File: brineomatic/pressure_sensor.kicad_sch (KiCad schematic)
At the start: 8 parts, among them J5 Conn_01x02

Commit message: getting closer.  added tds
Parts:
- renumbered C1 to C17, D1 to D18, J5 to J12, JP1 to JP2, R1 to R31, R9 to R32, R10 to R33, R2 to R34
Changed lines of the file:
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@@
 		(dnp no)
 		(fields_autoplaced yes)
-		(property "Reference" "#PWR01"
+		(property "Reference" "#PWR036"
 			(at 96.52 77.47 0)
 			(effects
@@
 		)
 		(instances
-			(project ""
-				(path "/96477ae2-ef08-48f3-8dd4-fe4478541f68/e7fd98b0-0753-4e9e-b57d-135c0c1a0b39"
-					(reference "#PWR01")
+			(project "brineomatic"
+				(path "/96477ae2-ef08-48f3-8dd4-fe4478541f68/c8ab4709-9ad5-4833-bb93-07e00d6a0170"
+					(reference "#PWR036")
+					(unit 1)
+				)
+				(path "/96477ae2-ef08-48f3-8dd4-fe4478541f68/e7fd98b0-0753-4e9e-b57d-135c0c1a0b39"
+					(reference "#PWR?")
 					(unit 1)
 				)
@@
 		(dnp no)
 		(fields_autoplaced yes)
-		(property "Reference" "JP1"
+		(property "Reference" "JP2"
 			(at 129.54 81.28 0)
 			(effects
@@
 		)
 		(instances
-			(project ""
-				(path "/96477ae2-ef08-48f3-8dd4-fe4478541f68/e7fd98b0-0753-4e9e-b57d-135c0c1a0b39"
-					(reference "JP1")
+			(project "brineomatic"
+				(path "/96477ae2-ef08-48f3-8dd4-fe4478541f68/c8ab4709-9ad5-4833-bb93-07e00d6a0170"
+					(reference "JP2")
+					(unit 1)
+				)
+				(path "/96477ae2-ef08-48f3-8dd4-fe4478541f68/e7fd98b0-0753-4e9e-b57d-135c0c1a0b39"
+					(reference "JP?")
 					(unit 1)
 				)
@@
 		(dnp no)
 		(fields_autoplaced yes)
-		(property "Reference" "#PWR05"
+		(property "Reference" "#PWR038"
 			(at 144.78 77.47 0)
 			(effects
@@
 		)
 		(instances
-			(project ""
-				(path "/96477ae2-ef08-48f3-8dd4-fe4478541f68/e7fd98b0-0753-4e9e-b57d-135c0c1a0b39"
-					(reference "#PWR05")
+			(project "brineomatic"
+				(path "/96477ae2-ef08-48f3-8dd4-fe4478541f68/c8ab4709-9ad5-4833-bb93-07e00d6a0170"
+					(reference "#PWR038")
+					(unit 1)
+				)
+				(path "/96477ae2-ef08-48f3-8dd4-fe4478541f68/e7fd98b0-0753-4e9e-b57d-135c0c1a0b39"
+					(reference "#PWR?")
 					(unit 1)
 				)
@@
 		(dnp no)
 		(fields_autoplaced yes)
-		(property "Reference" "#PWR02"
+		(property "Reference" "#PWR037"
 			(at 96.52 114.3 0)
 			(effects
@@
 		(instances
 			(project "brineomatic"
+				(path "/96477ae2-ef08-48f3-8dd4-fe4478541f68/c8ab4709-9ad5-4833-bb93-07e00d6a0170"
+					(reference "#PWR037")
+					(unit 1)
+				)
 				(path "/96477ae2-ef08-48f3-8dd4-fe4478541f68/e7fd98b0-0753-4e9e-b57d-135c0c1a0b39"
 					(reference "#PWR02")
@@
 		(dnp no)
 		(fields_autoplaced yes)
-		(property "Reference" "D1"
+		(property "Reference" "D18"
 			(at 147.32 86.36 90)
 			(effects
@@
 		(instances
 			(project "brineomatic"
+				(path "/96477ae2-ef08-48f3-8dd4-fe4478541f68/c8ab4709-9ad5-4833-bb93-07e00d6a0170"
+					(reference "D18")
+					(unit 1)
+				)
 				(path "/96477ae2-ef08-48f3-8dd4-fe4478541f68/e7fd98b0-0753-4e9e-b57d-135c0c1a0b39"
 					(reference "D1")
@@
 		(dnp no)
 		(fields_autoplaced yes)
-		(property "Reference" "R9"
+		(property "Reference" "R32"
 			(at 124.46 90.17 0)
 			(effects
@@
 		(instances
 			(project "brineomatic"
+				(path "/96477ae2-ef08-48f3-8dd4-fe4478541f68/c8ab4709-9ad5-4833-bb93-07e00d6a0170"
+					(reference "R32")
+					(unit 1)
+				)
 				(path "/96477ae2-ef08-48f3-8dd4-fe4478541f68/e7fd98b0-0753-4e9e-b57d-135c0c1a0b39"
 					(reference "R9")
@@
 		(dnp no)
 		(fields_autoplaced yes)
-		(property "Reference" "J5"
+		(property "Reference" "J12"
 			(at 87.63 78.74 0)
 			(effects
@@
 		)
 		(instances
-			(project ""
-				(path "/96477ae2-ef08-48f3-8dd4-fe4478541f68/e7fd98b0-0753-4e9e-b57d-135c0c1a0b39"
-					(reference "J5")
+			(project "brineomatic"
+				(path "/96477ae2-ef08-48f3-8dd4-fe4478541f68/c8ab4709-9ad5-4833-bb93-07e00d6a0170"
+					(reference "J12")
+					(unit 1)
+				)
+				(path "/96477ae2-ef08-48f3-8dd4-fe4478541f68/e7fd98b0-0753-4e9e-b57d-135c0c1a0b39"
+					(reference "J?")
 					(unit 1)
 				)
@@
 		(dnp no)
 		(fields_autoplaced yes)
-		(property "Reference" "R2"
+		(property "Reference" "R34"
 			(at 158.75 81.28 90)
 			(effects
@@
 		(instances
 			(project "brineomatic"
+				(path "/96477ae2-ef08-48f3-8dd4-fe4478541f68/c8ab4709-9ad5-4833-bb93-07e00d6a0170"
+					(reference "R34")
+					(unit 1)
+				)
 				(path "/96477ae2-ef08-48f3-8dd4-fe4478541f68/e7fd98b0-0753-4e9e-b57d-135c0c1a0b39"
 					(reference "R2")
@@
 		(dnp no)
 		(fields_autoplaced yes)
-		(property "Reference" "R10"
+		(property "Reference" "R33"
 			(at 124.46 97.79 0)
 			(effects
@@
 		(instances
 			(project "brineomatic"
+				(path "/96477ae2-ef08-48f3-8dd4-fe4478541f68/c8ab4709-9ad5-4833-bb93-07e00d6a0170"
+					(reference "R33")
+					(unit 1)
+				)
 				(path "/96477ae2-ef08-48f3-8dd4-fe4478541f68/e7fd98b0-0753-4e9e-b57d-135c0c1a0b39"
 					(reference "R10")
@@
 		(dnp no)
 		(fields_autoplaced yes)
-		(property "Reference" "R1"
+		(property "Reference" "R31"
 			(at 99.06 91.44 0)
 			(effects
@@
 		(instances
 			(project "brineomatic"
+				(path "/96477ae2-ef08-48f3-8dd4-fe4478541f68/c8ab4709-9ad5-4833-bb93-07e00d6a0170"
+					(reference "R31")
+					(unit 1)
+				)
 				(path "/96477ae2-ef08-48f3-8dd4-fe4478541f68/e7fd98b0-0753-4e9e-b57d-135c0c1a0b39"
 					(reference "R1")
@@
 		(on_board yes)
 		(dnp no)
-		(property "Reference" "C1"
+		(property "Reference" "C17"
 			(at 166.37 96.5263 0)
 			(effects
@@
 		(instances
 			(project "brineomatic"
+				(path "/96477ae2-ef08-48f3-8dd4-fe4478541f68/c8ab4709-9ad5-4833-bb93-07e00d6a0170"
+					(reference "C17")
+					(unit 1)
+				)
 				(path "/96477ae2-ef08-48f3-8dd4-fe4478541f68/e7fd98b0-0753-4e9e-b57d-135c0c1a0b39"
 					(reference "C1")

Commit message: starting to shape up, footprints etc
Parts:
- J12: value Conn_01x02 -> SENSOR; footprint (none) -> TerminalBlock_Phoenix:TerminalBlock_Phoenix_PT-1,5-2-3.5-H_1x02_P3.50mm_Horizontal
- JP2: footprint (none) -> Jumper:SolderJumper-2_P1.3mm_Open_RoundedPad1.0x1.5mm
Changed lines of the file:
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@@
 		(dnp no)
 		(fields_autoplaced yes)
-		(property "Reference" "#PWR036"
+		(property "Reference" "#PWR035"
 			(at 96.52 77.47 0)
 			(effects
@@
 			(project "brineomatic"
 				(path "/96477ae2-ef08-48f3-8dd4-fe4478541f68/c8ab4709-9ad5-4833-bb93-07e00d6a0170"
-					(reference "#PWR036")
-					(unit 1)
-				)
-				(path "/96477ae2-ef08-48f3-8dd4-fe4478541f68/e7fd98b0-0753-4e9e-b57d-135c0c1a0b39"
-					(reference "#PWR?")
+					(reference "#PWR035")
+					(unit 1)
+				)
+				(path "/96477ae2-ef08-48f3-8dd4-fe4478541f68/e7fd98b0-0753-4e9e-b57d-135c0c1a0b39"
+					(reference "#PWR06")
 					(unit 1)
 				)
@@
 			)
 		)
-		(property "Footprint" ""
+		(property "Footprint" "Jumper:SolderJumper-2_P1.3mm_Open_RoundedPad1.0x1.5mm"
 			(at 129.54 87.63 0)
 			(effects
@@
 				)
 				(path "/96477ae2-ef08-48f3-8dd4-fe4478541f68/e7fd98b0-0753-4e9e-b57d-135c0c1a0b39"
-					(reference "JP?")
+					(reference "JP1")
 					(unit 1)
 				)
@@
 		(dnp no)
 		(fields_autoplaced yes)
-		(property "Reference" "#PWR038"
+		(property "Reference" "#PWR037"
 			(at 144.78 77.47 0)
 			(effects
@@
 			(project "brineomatic"
 				(path "/96477ae2-ef08-48f3-8dd4-fe4478541f68/c8ab4709-9ad5-4833-bb93-07e00d6a0170"
-					(reference "#PWR038")
-					(unit 1)
-				)
-				(path "/96477ae2-ef08-48f3-8dd4-fe4478541f68/e7fd98b0-0753-4e9e-b57d-135c0c1a0b39"
-					(reference "#PWR?")
+					(reference "#PWR037")
+					(unit 1)
+				)
+				(path "/96477ae2-ef08-48f3-8dd4-fe4478541f68/e7fd98b0-0753-4e9e-b57d-135c0c1a0b39"
+					(reference "#PWR08")
 					(unit 1)
 				)
@@
 		(dnp no)
 		(fields_autoplaced yes)
-		(property "Reference" "#PWR037"
+		(property "Reference" "#PWR036"
 			(at 96.52 114.3 0)
 			(effects
@@
 			(project "brineomatic"
 				(path "/96477ae2-ef08-48f3-8dd4-fe4478541f68/c8ab4709-9ad5-4833-bb93-07e00d6a0170"
-					(reference "#PWR037")
-					(unit 1)
-				)
-				(path "/96477ae2-ef08-48f3-8dd4-fe4478541f68/e7fd98b0-0753-4e9e-b57d-135c0c1a0b39"
-					(reference "#PWR02")
+					(reference "#PWR036")
+					(unit 1)
+				)
+				(path "/96477ae2-ef08-48f3-8dd4-fe4478541f68/e7fd98b0-0753-4e9e-b57d-135c0c1a0b39"
+					(reference "#PWR07")
 					(unit 1)
 				)
@@
 				)
 				(path "/96477ae2-ef08-48f3-8dd4-fe4478541f68/e7fd98b0-0753-4e9e-b57d-135c0c1a0b39"
-					(reference "R9")
+					(reference "R2")
 					(unit 1)
 				)
@@
 			)
 		)
-		(property "Value" "Conn_01x02"
+		(property "Value" "SENSOR"
 			(at 87.63 81.28 0)
 			(effects
@@
 			)
 		)
-		(property "Footprint" ""
+		(property "Footprint" "TerminalBlock_Phoenix:TerminalBlock_Phoenix_PT-1,5-2-3.5-H_1x02_P3.50mm_Horizontal"
 			(at 87.63 85.09 0)
 			(effects
@@
 				)
 				(path "/96477ae2-ef08-48f3-8dd4-fe4478541f68/e7fd98b0-0753-4e9e-b57d-135c0c1a0b39"
-					(reference "J?")
+					(reference "J1")
 					(unit 1)
 				)
@@
 				)
 				(path "/96477ae2-ef08-48f3-8dd4-fe4478541f68/e7fd98b0-0753-4e9e-b57d-135c0c1a0b39"
-					(reference "R2")
+					(reference "R4")
 					(unit 1)
 				)
@@
 				)
 				(path "/96477ae2-ef08-48f3-8dd4-fe4478541f68/e7fd98b0-0753-4e9e-b57d-135c0c1a0b39"
-					(reference "R10")
-					(unit 1)
-				)
+					(reference "R3")
+					(unit 1)
+				)

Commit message: starting to look good.
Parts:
- removed JP2: For Testing, Jumper:SolderJumper-2_P1.3mm_Open_RoundedPad1.0x1.5mm, symbol Jumper:SolderJumper_2_Open
- removed R32: 10.2K 0.1%, Resistor_SMD:R_1206_3216Metric_Pad1.30x1.75mm_HandSolder, symbol Device:R_Small_US
- removed R33: 19.8K 0.1%, Resistor_SMD:R_1206_3216Metric_Pad1.30x1.75mm_HandSolder, symbol Device:R_Small_US
- J12: value SENSOR -> PRESSURE; footprint TerminalBlock_Phoenix:TerminalBlock_Phoenix_PT-1,5-2-3.5-H_1x02_P3.50mm_Horizontal -> Connector_JST:JST_PH_S2B-PH-K_1x02_P2.00mm_Horizontal
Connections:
- net at J12.2 (Pin_2), R31.2: now also D18.3 (COM), R34.1
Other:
- moved on the sheet: C17, D18, R34

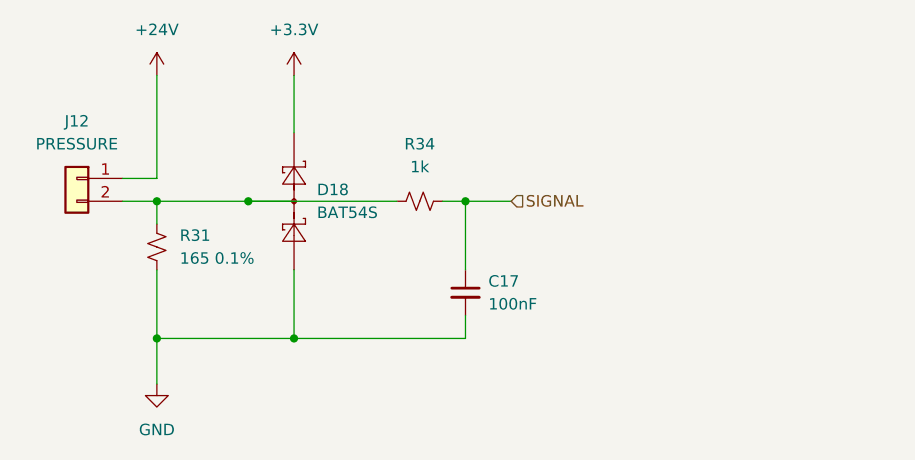
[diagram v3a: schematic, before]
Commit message: updated bom and prepping for Rev A
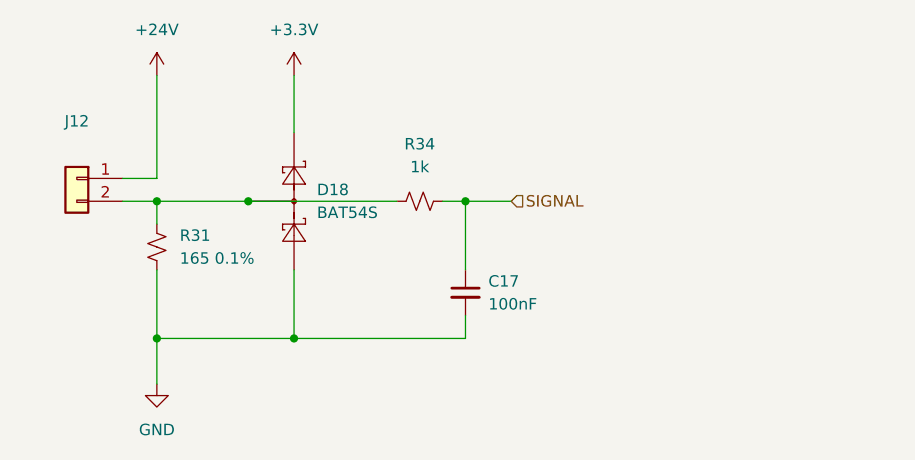
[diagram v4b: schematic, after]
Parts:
- J12: value PRESSURE -> ~; LCSC (none) -> C173752
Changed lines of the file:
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@@
 			)
 		)
-		(property "Value" "PRESSURE"
+		(property "Value" "~"
 			(at 87.63 81.28 0)
 			(effects
@@
 			(at 87.63 85.09 0)
 			(effects
+				(font
+					(size 1.27 1.27)
+				)
+				(hide yes)
+			)
+		)
+		(property "LCSC" "C173752"
+			(at 87.63 85.09 0)
+			(effects

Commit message: updates parts, footprints, etc.  ready for production.
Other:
- moved on the sheet: C17, R31
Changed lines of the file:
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@@
 	(wire
 		(pts
-			(xy 130.81 87.63) (xy 130.81 95.25)
+			(xy 130.81 87.63) (xy 130.81 92.71)
 		)
 		(stroke
@@
 	(wire
 		(pts
-			(xy 96.52 87.63) (xy 96.52 90.17)
+			(xy 96.52 87.63) (xy 96.52 92.71)
 		)
 		(stroke
@@
 	(wire
 		(pts
-			(xy 130.81 100.33) (xy 130.81 102.87)
+			(xy 130.81 97.79) (xy 130.81 102.87)
 		)
 		(stroke
@@
 	(wire
 		(pts
-			(xy 96.52 95.25) (xy 96.52 102.87)
+			(xy 96.52 97.79) (xy 96.52 102.87)
 		)
 		(stroke
@@
 	(symbol
 		(lib_id "Device:R_Small_US")
-		(at 96.52 92.71 180)
+		(at 96.52 95.25 180)
 		(unit 1)
 		(exclude_from_sim no)
@@
 		(fields_autoplaced yes)
 		(property "Reference" "R31"
-			(at 99.06 91.44 0)
+			(at 99.06 93.98 0)
 			(effects
 				(font
@@
 		)
 		(property "Value" "165 0.1%"
-			(at 99.06 93.98 0)
+			(at 99.06 96.52 0)
 			(effects
 				(font
@@
 		)
 		(property "Footprint" "Resistor_SMD:R_1206_3216Metric_Pad1.30x1.75mm_HandSolder"
-			(at 96.52 92.71 0)
+			(at 96.52 95.25 0)
 			(effects
 				(font
@@
 		)
 		(property "Datasheet" "~"
-			(at 96.52 92.71 0)
+			(at 96.52 95.25 0)
 			(effects
 				(font
@@
 		)
 		(property "Description" ""
-			(at 96.52 92.71 0)
+			(at 96.52 95.25 0)
 			(effects
 				(font
@@
 		)
 		(property "LCSC" "C870446"
-			(at 96.52 92.71 0)
+			(at 96.52 95.25 0)
 			(effects
 				(font
@@
 	(symbol
 		(lib_id "Device:C_Small")
-		(at 130.81 97.79 0)
+		(at 130.81 95.25 0)
 		(unit 1)
 		(exclude_from_sim no)
@@
 		(dnp no)
 		(property "Reference" "C17"
+			(at 133.35 93.9863 0)
+			(effects
+				(font
+					(size 1.27 1.27)
+				)
+				(justify left)
+			)
+		)
+		(property "Value" "100nF"
 			(at 133.35 96.5263 0)
 			(effects
@@
 			)
 		)
-		(property "Value" "100nF"
-			(at 133.35 99.0663 0)
-			(effects
-				(font
-					(size 1.27 1.27)
-				)
-				(justify left)
-			)
-		)
 		(property "Footprint" "Capacitor_SMD:C_0805_2012Metric_Pad1.18x1.45mm_HandSolder"
-			(at 130.81 97.79 0)
+			(at 130.81 95.25 0)
 			(effects
 				(font
@@
 		)
 		(property "Datasheet" "~"
-			(at 130.81 97.79 0)
+			(at 130.81 95.25 0)
 			(effects
 				(font
@@
 		)
 		(property "Description" ""
-			(at 130.81 97.79 0)
+			(at 130.81 95.25 0)
 			(effects
 				(font
@@
 		)
 		(property "Mouser" ""
-			(at 130.81 97.79 0)
+			(at 130.81 95.25 0)
 			(effects
 				(font
@@
 		)
 		(property "LCSC" "C49678"
-			(at 130.81 97.79 0)
-			(effects
-				(font
+			(at 130.81 95.25 0)
+			(effects
+				(font

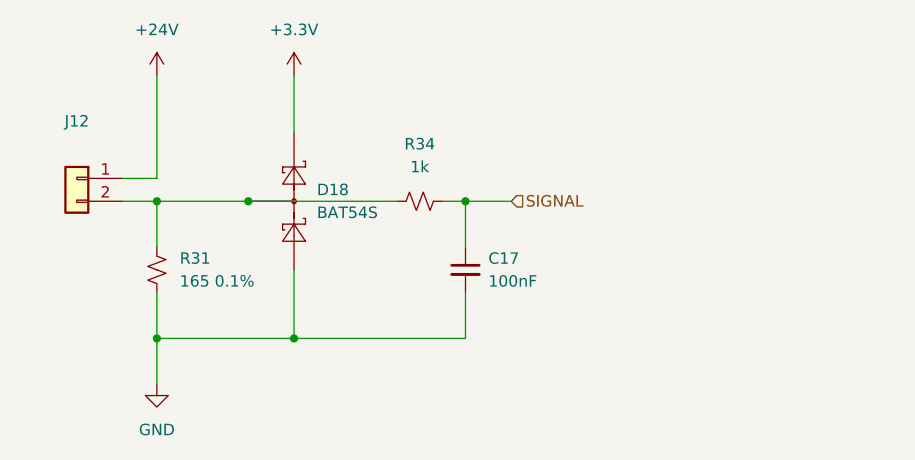
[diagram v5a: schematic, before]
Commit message: fixed bat54s placement.
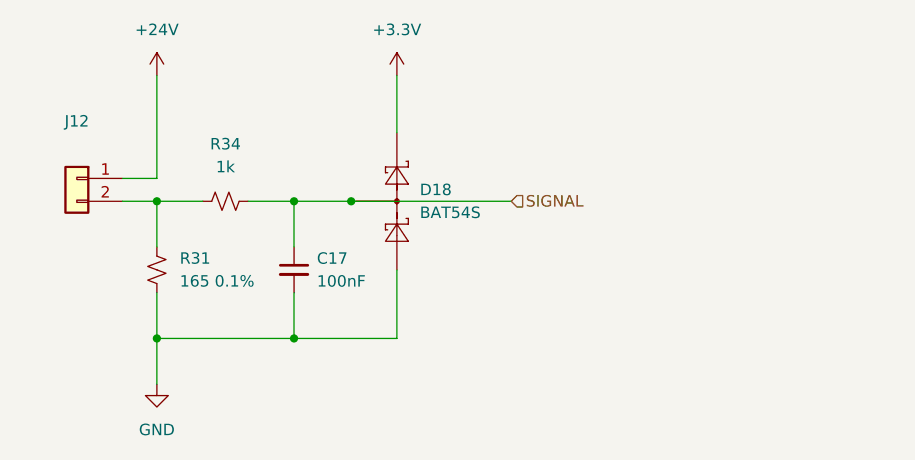
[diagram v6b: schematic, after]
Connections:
- net SIGNAL: now also D18.3 (COM)
- net at J12.2 (Pin_2), R31.2, R34.1: no longer D18.3 (COM)
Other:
- moved on the sheet: C17, D18, R34
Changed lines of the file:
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@@
 	(paper "A4")
+	(junction
+		(at 118.11 87.63)
+		(diameter 0)
+		(color 0 0 0 0)
+	)
+	(junction
+		(at 96.52 87.63)
+		(diameter 0)
+		(color 0 0 0 0)
+	)
 	(junction
 		(at 111.76 102.87)
@@
 	)
 	(junction
-		(at 130.81 87.63)
-		(diameter 0)
-		(color 0 0 0 0)
-	)
-	(junction
-		(at 96.52 87.63)
+		(at 111.76 87.63)
 		(diameter 0)
 		(color 0 0 0 0)
@@
 		(color 0 0 0 0)
 	)
-	(junction
-		(at 106.68 87.63)
-		(diameter 0)
-		(color 0 0 0 0)
-	)
-	(wire
-		(pts
-			(xy 130.81 87.63) (xy 135.89 87.63)
-		)
-		(stroke
-			(width 0)
-			(type default)
-		)
-	)
-	(wire
-		(pts
-			(xy 128.27 87.63) (xy 130.81 87.63)
-		)
-		(stroke
-			(width 0)
-			(type default)
-		)
-	)
-	(wire
-		(pts
-			(xy 111.76 73.66) (xy 111.76 80.01)
-		)
-		(stroke
-			(width 0)
-			(type default)
-		)
-	)
-	(wire
-		(pts
-			(xy 106.68 87.63) (xy 123.19 87.63)
-		)
-		(stroke
-			(width 0)
-			(type default)
-		)
-	)
-	(wire
-		(pts
-			(xy 111.76 102.87) (xy 111.76 95.25)
-		)
-		(stroke
-			(width 0)
-			(type default)
-		)
-	)
-	(wire
-		(pts
-			(xy 111.76 102.87) (xy 130.81 102.87)
+	(wire
+		(pts
+			(xy 111.76 87.63) (xy 118.11 87.63)
+		)
+		(stroke
+			(width 0)
+			(type default)
+		)
+	)
+	(wire
+		(pts
+			(xy 123.19 73.66) (xy 123.19 80.01)
+		)
+		(stroke
+			(width 0)
+			(type default)
+		)
+	)
+	(wire
+		(pts
+			(xy 123.19 102.87) (xy 123.19 95.25)
 		)
 		(stroke
@@
 	(wire
 		(pts
+			(xy 111.76 102.87) (xy 123.19 102.87)
+		)
+		(stroke
+			(width 0)
+			(type default)
+		)
+	)
+	(wire
+		(pts
 			(xy 92.71 87.63) (xy 96.52 87.63)
 		)
@@
 	(wire
 		(pts
-			(xy 130.81 87.63) (xy 130.81 92.71)
+			(xy 118.11 87.63) (xy 135.89 87.63)
+		)
+		(stroke
+			(width 0)
+			(type default)
+		)
+	)
+	(wire
+		(pts
+			(xy 111.76 87.63) (xy 111.76 92.71)
 		)
 		(stroke
@@
 	(wire
 		(pts
-			(xy 130.81 97.79) (xy 130.81 102.87)
+			(xy 111.76 97.79) (xy 111.76 102.87)
+		)
+		(stroke
+			(width 0)
+			(type default)
+		)
+	)
+	(wire
+		(pts
+			(xy 106.68 87.63) (xy 111.76 87.63)
 		)
 		(stroke
@@
 	(wire
 		(pts
-			(xy 96.52 87.63) (xy 106.68 87.63)
-		)
-		(stroke
-			(width 0)
-			(type default)
-		)
-	)
-	(wire
-		(pts
 			(xy 96.52 97.79) (xy 96.52 102.87)
+		)
+		(stroke
+			(width 0)
+			(type default)
+		)
+	)
+	(wire
+		(pts
+			(xy 96.52 87.63) (xy 101.6 87.63)
 		)
 		(stroke
@@
 	(symbol
 		(lib_id "power:+3.3V")
-		(at 111.76 73.66 0)
+		(at 123.19 73.66 0)
 		(unit 1)
 		(exclude_from_sim no)
@@
 		(fields_autoplaced yes)
 		(property "Reference" "#PWR037"
-			(at 111.76 77.47 0)
+			(at 123.19 77.47 0)
 			(effects
 				(font
@@
 		)
 		(property "Value" "+3.3V"
-			(at 111.76 68.58 0)
+			(at 123.19 68.58 0)
 			(effects
 				(font
@@
 		)
 		(property "Footprint" ""
-			(at 111.76 73.66 0)
+			(at 123.19 73.66 0)
 			(effects
 				(font
@@
 		)
 		(property "Datasheet" ""
-			(at 111.76 73.66 0)
+			(at 123.19 73.66 0)
 			(effects
 				(font
@@
 		)
 		(property "Description" "Power symbol creates a global label with name \"+3.3V\""
-			(at 111.76 73.66 0)
+			(at 123.19 73.66 0)
 			(effects
 				(font
@@
 	(symbol
 		(lib_id "Diode:BAT54S")
-		(at 111.76 87.63 270)
+		(at 123.19 87.63 270)
 		(mirror x)
 		(unit 1)
@@
 		(fields_autoplaced yes)
 		(property "Reference" "D18"
-			(at 114.3 86.36 90)
+			(at 125.73 86.36 90)
 			(effects
 				(font
@@
 		)
 		(property "Value" "BAT54S"
-			(at 114.3 88.9 90)
+			(at 125.73 88.9 90)
 			(effects
 				(font
@@
 		)
 		(property "Footprint" "Package_TO_SOT_SMD:SOT-23"
-			(at 114.935 85.725 0)
+			(at 126.365 85.725 0)
 			(effects
 				(font
@@
 		)
 		(property "Datasheet" "https://www.diodes.com/assets/Datasheets/ds11005.pdf"
-			(at 111.76 90.678 0)
+			(at 123.19 90.678 0)
 			(effects
 				(font
@@
 		)
 		(property "Description" ""
-			(at 111.76 87.63 0)
+			(at 123.19 87.63 0)
 			(effects
 				(font
@@
 		)
 		(property "LCSC" "C727126"
-			(at 111.76 87.63 90)
+			(at 123.19 87.63 90)
 			(effects
 				(font
@@
 	(symbol
 		(lib_id "Device:R_Small_US")
-		(at 125.73 87.63 90)
+		(at 104.14 87.63 90)
 		(unit 1)
 		(exclude_from_sim no)
@@
 		(fields_autoplaced yes)
 		(property "Reference" "R34"
-			(at 125.73 81.28 90)
+			(at 104.14 81.28 90)
 			(effects
 				(font
@@
 		)
 		(property "Value" "1k"
-			(at 125.73 83.82 90)
+			(at 104.14 83.82 90)
 			(effects
 				(font
@@
 		)
 		(property "Footprint" "Resistor_SMD:R_0805_2012Metric_Pad1.20x1.40mm_HandSolder"
-			(at 125.73 87.63 0)
+			(at 104.14 87.63 0)
 			(effects
 				(font
@@
 		)
 		(property "Datasheet" "~"
-			(at 125.73 87.63 0)
+			(at 104.14 87.63 0)
 			(effects
 				(font
@@
 		)
 		(property "Description" ""
-			(at 125.73 87.63 0)
+			(at 104.14 87.63 0)
 			(effects
 				(font
@@
 		)
 		(property "LCSC" "C95781"
-			(at 125.73 87.63 0)
+			(at 104.14 87.63 0)
 			(effects
 				(font
@@
 	(symbol
 		(lib_id "Device:C_Small")
-		(at 130.81 95.25 0)
+		(at 111.76 95.25 0)
 		(unit 1)
 		(exclude_from_sim no)
@@
 		(dnp no)
 		(property "Reference" "C17"
-			(at 133.35 93.9863 0)
+			(at 114.3 93.9863 0)
 			(effects
 				(font
@@
 		)
 		(property "Value" "100nF"
-			(at 133.35 96.5263 0)
+			(at 114.3 96.5263 0)
 			(effects
 				(font
@@
 		)
 		(property "Footprint" "Capacitor_SMD:C_0805_2012Metric_Pad1.18x1.45mm_HandSolder"
-			(at 130.81 95.25 0)
+			(at 111.76 95.25 0)
 			(effects
 				(font
@@
 		)
 		(property "Datasheet" "~"
-			(at 130.81 95.25 0)
+			(at 111.76 95.25 0)
 			(effects
 				(font
@@
 		)
 		(property "Description" ""
-			(at 130.81 95.25 0)
+			(at 111.76 95.25 0)
 			(effects
 				(font
@@
 		)
 		(property "Mouser" ""
-			(at 130.81 95.25 0)
+			(at 111.76 95.25 0)
 			(effects
 				(font
@@
 		)
 		(property "LCSC" "C49678"
-			(at 130.81 95.25 0)
-			(effects
-				(font
+			(at 111.76 95.25 0)
+			(effects
+				(font
